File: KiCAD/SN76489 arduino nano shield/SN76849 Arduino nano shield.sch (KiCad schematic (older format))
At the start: 18 parts, among them J1 Arduino_sn, J2 audio_debug, J4 I2C, J5 LOGO, J6 gat1, J7 gat2, J8 geluid_uit, U1 PCF8574, U2 LM358, U3 SN76489

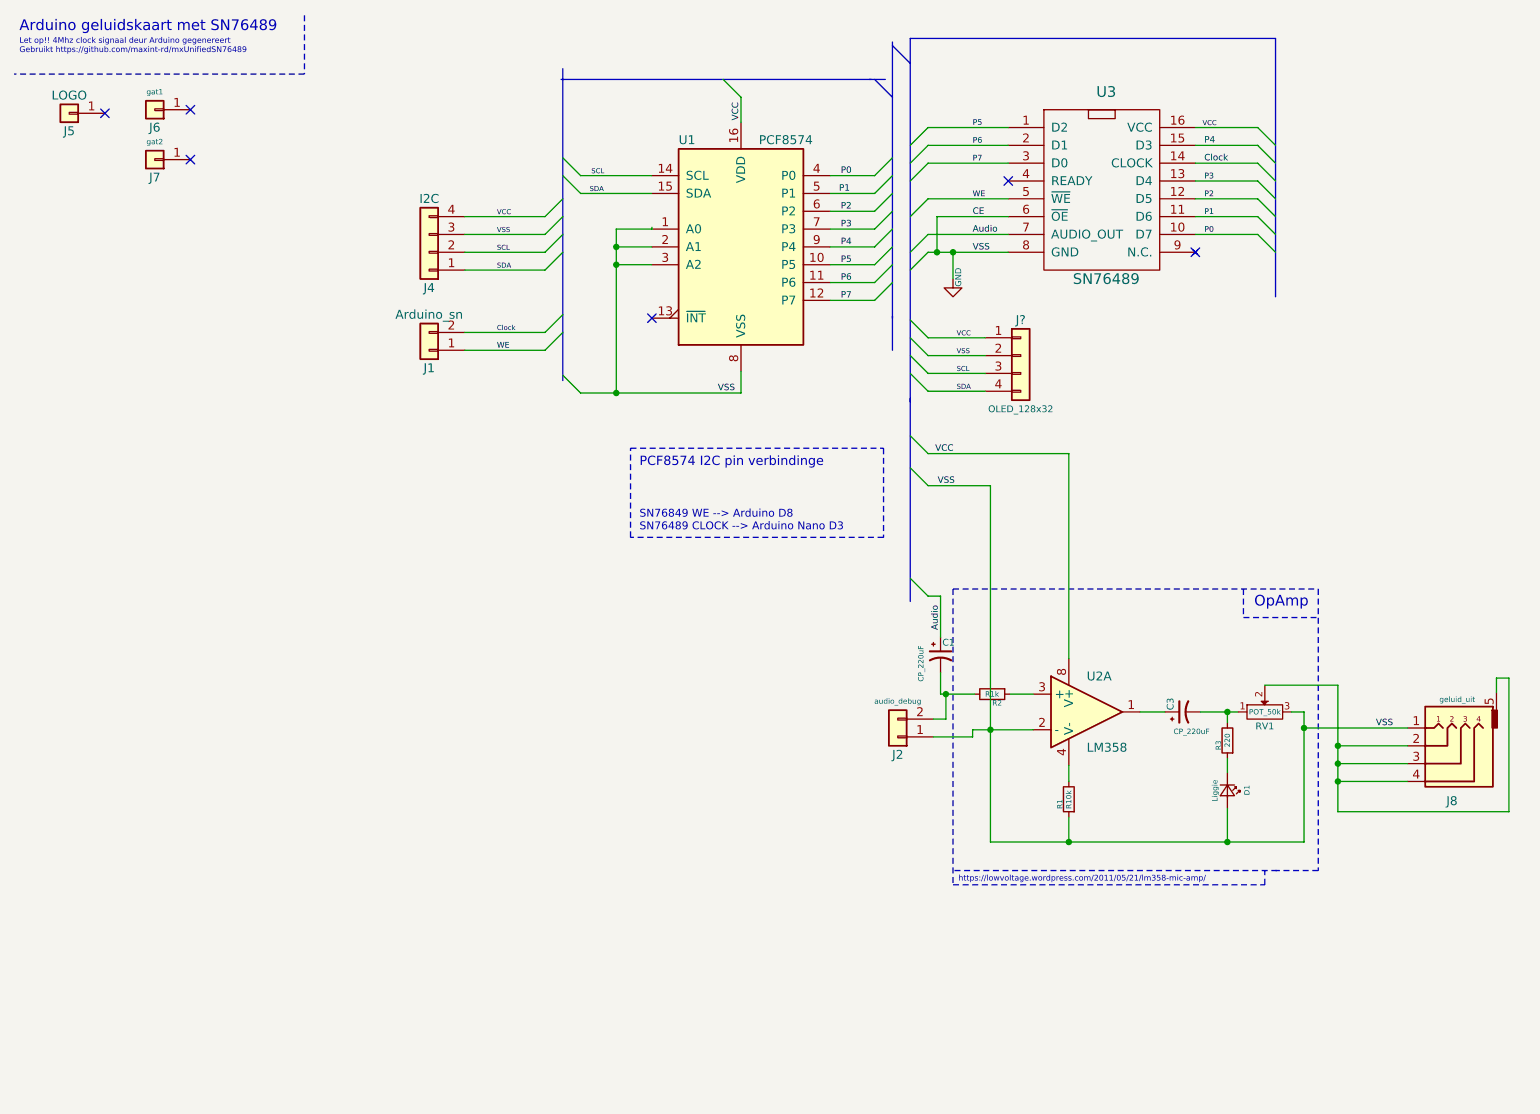
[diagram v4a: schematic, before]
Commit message: 20180719 0.7.03 OLED
Groot bugfix;

POTmeter verbinding
LM358 nu dual op
PWM pin is verbonde met LM358 out2
Geluidsuitgang debug in stereo
OLED skerm I2c toegevoegd.
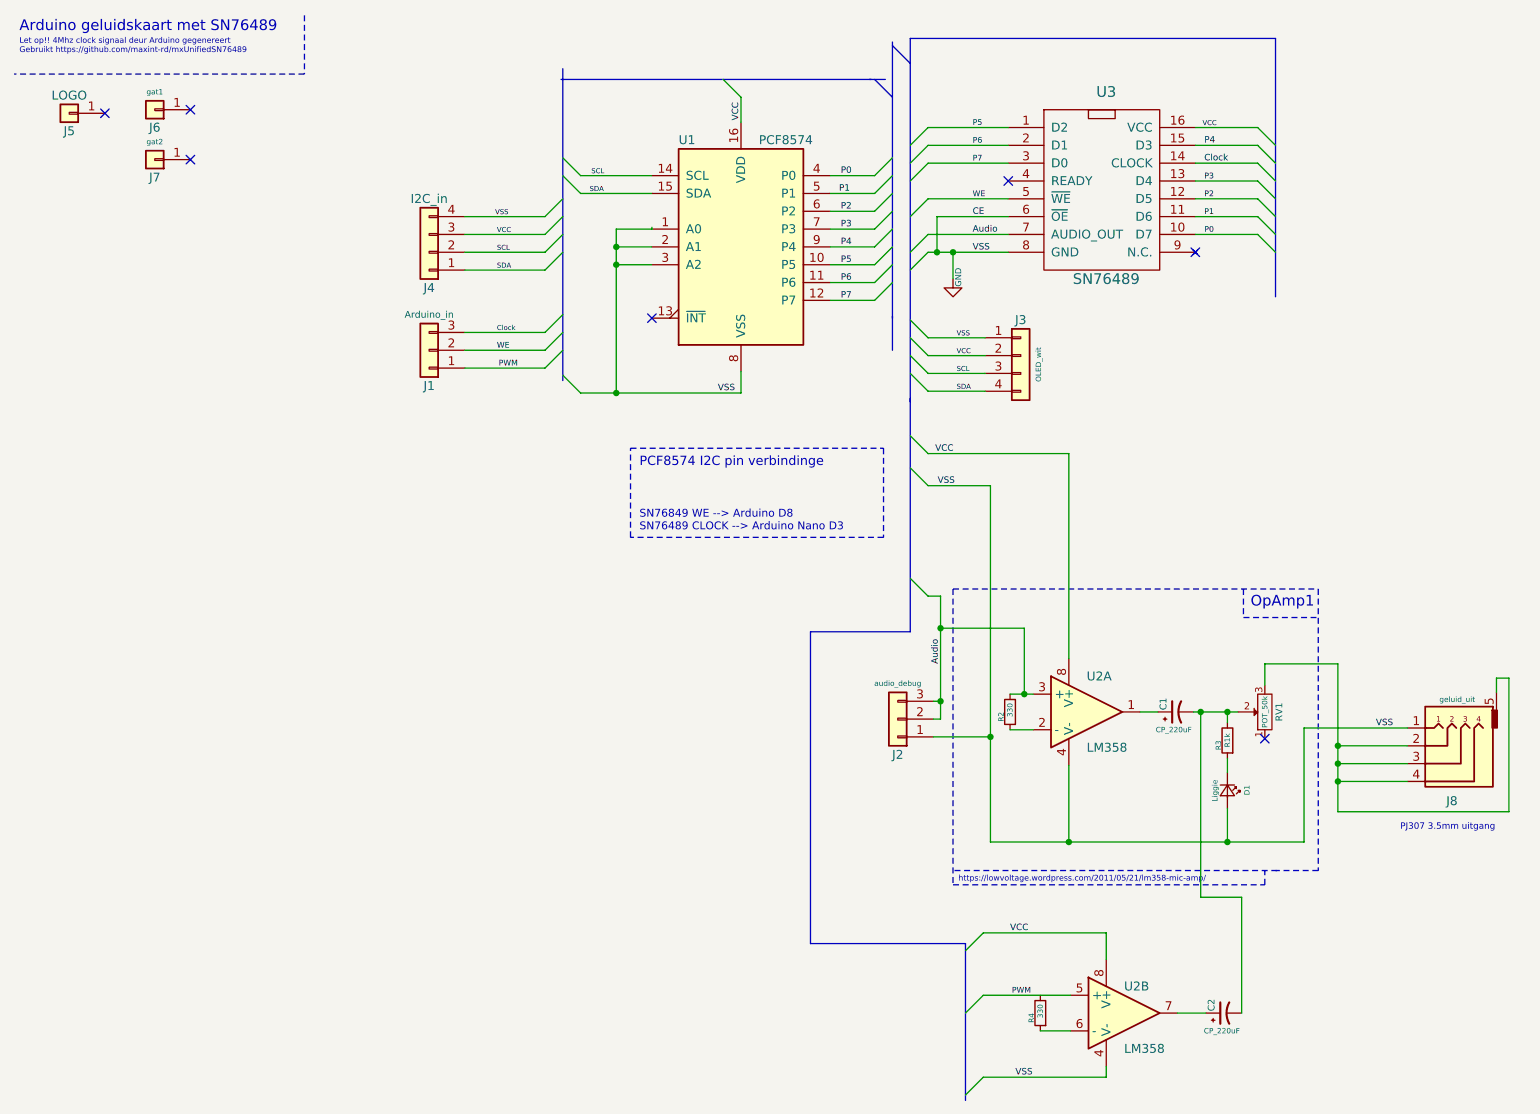
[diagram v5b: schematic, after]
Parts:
- removed C3: CP_220uF, Capacitors_THT:CP_Radial_D8.0mm_P2.50mm, symbol CP1_Small
- removed J1: Arduino_sn, Pin_Headers:Pin_Header_Angled_1x02_Pitch2.54mm, symbol Conn_01x02
- removed J2: audio_debug, Pin_Headers:Pin_Header_Angled_1x02_Pitch2.54mm, symbol Conn_01x02
- removed R1: R10k, w_pth_resistors:RC03, symbol R_Small
- added C2: CP_220uF, Capacitors_THT:CP_Radial_D8.0mm_P2.50mm, symbol CP1_Small
- added J1: Arduino_in, Pin_Headers:Pin_Header_Angled_1x04_Pitch2.54mm, symbol Conn_01x03
- added J2: audio_debug, Pin_Headers:Pin_Header_Angled_1x03_Pitch2.54mm, symbol Conn_01x03
- added R4: 330, w_pth_resistors:RC03, symbol R_Small
- added unit 2 of U2
- J3: renamed from J?; value OLED_128x32 -> OLED_wit
- J4: value I2C -> I2C_in
- R2: value R1k -> 330
- R3: value 220 -> R1k
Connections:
- net Audio: now also R2.2, U2.3 (+), J2.2 (Pin_2), J2.3 (Pin_3); no longer C1.1
- net Clock: now also J1.3 (Pin_3)
- net GND: now also J3.1 (Pin_1), J4.4 (Pin_4), U2.4 (V-), J2.1 (Pin_1), U2.4 (V-); no longer J3.2 (Pin_2), J4.3 (Pin_3), RV1.3, U2.2 (-)
- net VCC: now also J3.2 (Pin_2), J4.3 (Pin_3), U2.8 (V+); no longer J3.1 (Pin_1), J4.4 (Pin_4)
- net WE: now also J1.2 (Pin_2)
- net at U2.1: now also C1.1
- net at RV1.1: no longer R3.2
- net at J8.2, J8.3, J8.4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: now also RV1.3; no longer RV1.2
- net at R2.1: now also U2.2 (-); no longer U2.3 (+)
- net at C1.2: now also R3.2, RV1.2, C2.2; no longer R2.2
- new net: R4.1, U2.6 (-)
- new net: C2.1, U2.7
- new net PWM: J1.1 (Pin_1), U2.5 (+)
- no-connect marks 6 -> 7
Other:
- note added: "OpAmp1"
- note added: "PJ307 3.5mm uitgang"
- note removed: "OpAmp"
- moved on the sheet: C1, R2, RV1
